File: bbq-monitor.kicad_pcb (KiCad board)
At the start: 4 copper layers, 48.5 x 43.3 mm, 51 parts, among them J1 Power, J2 USB_B_Mini, J3 Thermocouple, Q1 AO3401A, Q2 BC847, Q3 BC847, SW1 SW_Push, U1 ESP32-WROOM-32D, U2 TPS62132, U3 CP2104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

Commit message: Gave it a bit of a tidy up
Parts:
- removed the H4 at (190.8, 63.0)
- added H2: TL, MountingHole:MountingHole_3.2mm_M3_Pad_Via, F.Cu at (150.9, 62.7)
- R14: value 820k -> 82K
- R15: value 270k -> 27k
- moved H4 40.0 mm to (190.8, 63.0)
- moved R5 15.9 mm to (171.1, 83.4), turned to 90 degrees
- moved D2 14.0 mm to (173.1, 83.3)
- moved R12 2.45 mm to (187.7, 73.2), turned to 180 degrees
- moved C10 0.66 mm to (164.5, 95.3)
- moved R9 0.47 mm to (172.5, 65.8), turned to 270 degrees
- moved H1 0.08 mm to (151.0, 96.9), turned to 0 degrees
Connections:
- net Net-(D1-Pad2) renamed LED2
- D2 pad 2: Net-(D2-Pad2) -> LED1
- U1 pad 13: Net-(D2-Pad2) -> Net-(U1-Pad13)
- U1 pad 16: Net-(U1-Pad16) -> LED1
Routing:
- net Net-(D2-Pad2): track 16.3 -> 0.00 mm
- net +3V3: track 44.9 -> 51.9 mm, vias 13 -> 16
- net TEMP_HUMID_SEN: track 19.3 -> 14.3 mm
- net RESET: track 39.4 -> 44.1 mm
- net LED1: track 0.00 -> 3.44 mm
- net +5V: track 29.6 -> 27.4 mm
- net Net-(J3-Pad1): track 9.30 -> 7.73 mm
- net Net-(U1-Pad13): track 0.00 -> 0.61 mm
- net GND: vias 109 -> 141
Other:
- board text added: "ESP32-BBQ"

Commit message: updated gerbers
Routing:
- net /DIFF+: track 30.5 -> 31.9 mm
- net /DIFF-: track 29.5 -> 30.7 mm

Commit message: up
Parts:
- removed C10, C12, C14: 100n, Capacitor_SMD:C_0603_1608Metric
- removed C13, C15: 10n, Capacitor_SMD:C_0603_1608Metric
- removed C16: 100n, Capacitor_SMD:C_0402_1005Metric
- removed C17: 10u, Capacitor_SMD:C_0402_1005Metric
- removed H4: TR, MountingHole:MountingHole_3.2mm_M3_Pad_Via
- removed U5: AD8495, Package_SO:MSOP-8_3x3mm_P0.65mm
- removed U6: DHT11, Sensor:Aosong_DHT11_5.5x12.0_P2.54mm
- added C9: 100n, Capacitor_SMD:C_0603_1608Metric, F.Cu at (206.5, 86.8)
- added D3: RED, LED_SMD:LED_0603_1608Metric, F.Cu at (173.6, 113.1)
- added D4: RED, LED_SMD:LED_0603_1608Metric, F.Cu at (201.4, 113.4)
- added D5: RED, LED_SMD:LED_0603_1608Metric, F.Cu at (196.5, 113.4)
- added D6: D_Zener, Diode_SMD:D_1206_3216Metric, F.Cu at (169.7, 107.1)
- added D7: D_Schottky, Diode_SMD:D_1206_3216Metric, F.Cu at (173.2, 101.1)
- added IC1: MAX6675, hardware libraries:SO08, F.Cu at (202.9, 90.1)
- added Q4: AO3401A, Package_TO_SOT_SMD:SOT-23, F.Cu at (172.8, 104.0)
- J1: value Power -> Battery Power
- R10, R11, R9: value 1M -> 220
- R13: value 100 -> 10k
- moved H1 60.3 mm to (208.7, 114.3)
- moved R11 52.0 mm to (198.2, 113.4)
- moved J1 50.2 mm to (166.1, 112.0)
- moved R10 50.1 mm to (199.8, 113.4)
- moved R9 47.4 mm to (172.1, 113.2)
- moved J3 46.9 mm to (205.8, 97.7), turned to 90 degrees
- moved F1 44.2 mm to (166.2, 105.3), turned to 270 degrees
- moved J2 43.7 mm to (188.2, 110.5), turned to 0 degrees
- moved Q1 41.5 mm to (169.2, 104.0)
- moved C8 40.9 mm to (175.5, 108.5), turned to 270 degrees
- moved L1 39.9 mm to (179.9, 108.6)
- moved C1 39.7 mm to (175.3, 104.0), turned to 270 degrees
- moved U2 39.2 mm to (180.1, 104.8), turned to 180 degrees
- moved Q2 38.7 mm to (196.3, 102.8), turned to 90 degrees
- moved Q3 38.6 mm to (200.0, 102.8)
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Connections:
- net Net-(F1-Pad2) renamed BATT_PWR
- C1 pad 1: /BATT -> Net-(C1-Pad1)
- C2 pad 1: /BATT -> Net-(C1-Pad1)
- J2 pad 1: +5V -> USB_PWR
- J3 pad 1: Net-(J3-Pad1) -> GND
- J3 pad 2: Net-(J3-Pad2) -> Net-(IC1-Pad3)
- Q1 pad 2: /BATT -> BATT_SAFE
- R10 pad 1: Net-(J3-Pad2) -> TX_LED
- R10 pad 2: /Thermocouple_INPUT_FILTERED+ -> Net-(D4-Pad1)
- R11 pad 1: Net-(J3-Pad1) -> RX_LED
- R11 pad 2: /Thermocouple_INPUT_FILTERED- -> Net-(D5-Pad1)
- R12 pad 1: +3V3 -> GND
- R12 pad 2: TEMP_HUMID_SEN -> USB_PWR
- R14 pad 1: /BATT -> BATT_SAFE
- R9 pad 2: Net-(J3-Pad1) -> Net-(D3-Pad1)
- U1 pad 11: THERMOCOUPLE -> Net-(U1-Pad11)
- U1 pad 29: Net-(U1-Pad29) -> THERMO_SPI_CS
- U1 pad 30: Net-(U1-Pad30) -> THERMO_SPI_CLK
- U1 pad 31: Net-(U1-Pad31) -> THERMO_SPI_DO
- U1 pad 6: TEMP_HUMID_SEN -> Net-(U1-Pad6)
- U2 pad 10: /BATT -> Net-(C1-Pad1)
- U2 pad 11: /BATT -> Net-(C1-Pad1)
- U2 pad 12: /BATT -> Net-(C1-Pad1)
- U2 pad 13: /BATT -> Net-(C1-Pad1)
- U3 pad 13: Net-(U3-Pad13) -> RX_LED
- U3 pad 14: Net-(U3-Pad14) -> TX_LED
- U3 pad 8: +5V -> USB_PWR
- U4 pad 5: +5V -> USB_PWR
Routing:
- net USB_PWR: track 0.00 -> 51.1 mm
- net GND: track 71.2 -> 117.4 mm, vias 141 -> 68
- net /DIFF+: track 31.9 -> 2.22 mm
- net /DIFF-: track 30.7 -> 2.27 mm
- net +5V: track 27.4 -> 0.00 mm, vias 2 -> 0
- net /BATT: track 26.2 -> 0.00 mm
- net RX_CP+: track 1.78 -> 26.7 mm
- net GPIO0: track 30.3 -> 9.16 mm
- net TX_CP-: track 4.18 -> 24.9 mm
- net BATT_LEVEL: track 22.3 -> 3.78 mm
- net BATT_SAFE: track 0.00 -> 18.1 mm
- net TEMP_HUMID_SEN: track 14.3 -> 0.00 mm
- net Net-(C1-Pad1): track 0.00 -> 14.1 mm
- net D+: track 3.68 -> 15.7 mm, vias 0 -> 2
- net THERMO_SPI_DO: track 0.00 -> 10.2 mm
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- removed copper zone on B.Cu, net GND
- removed copper zone on F.Cu, net GND
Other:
- board size 48.5 x 43.3 mm -> 47 x 39.1 mm
- board text added: "BBQ-ESP32"
- board text added: "H.D."
- board text removed: "+"
- board text removed: "ESP32-BBQ"
- board text removed: "Harry Dobbs Version: 1.0"
- board text removed: "POWER"
- board text removed: "TEMP"

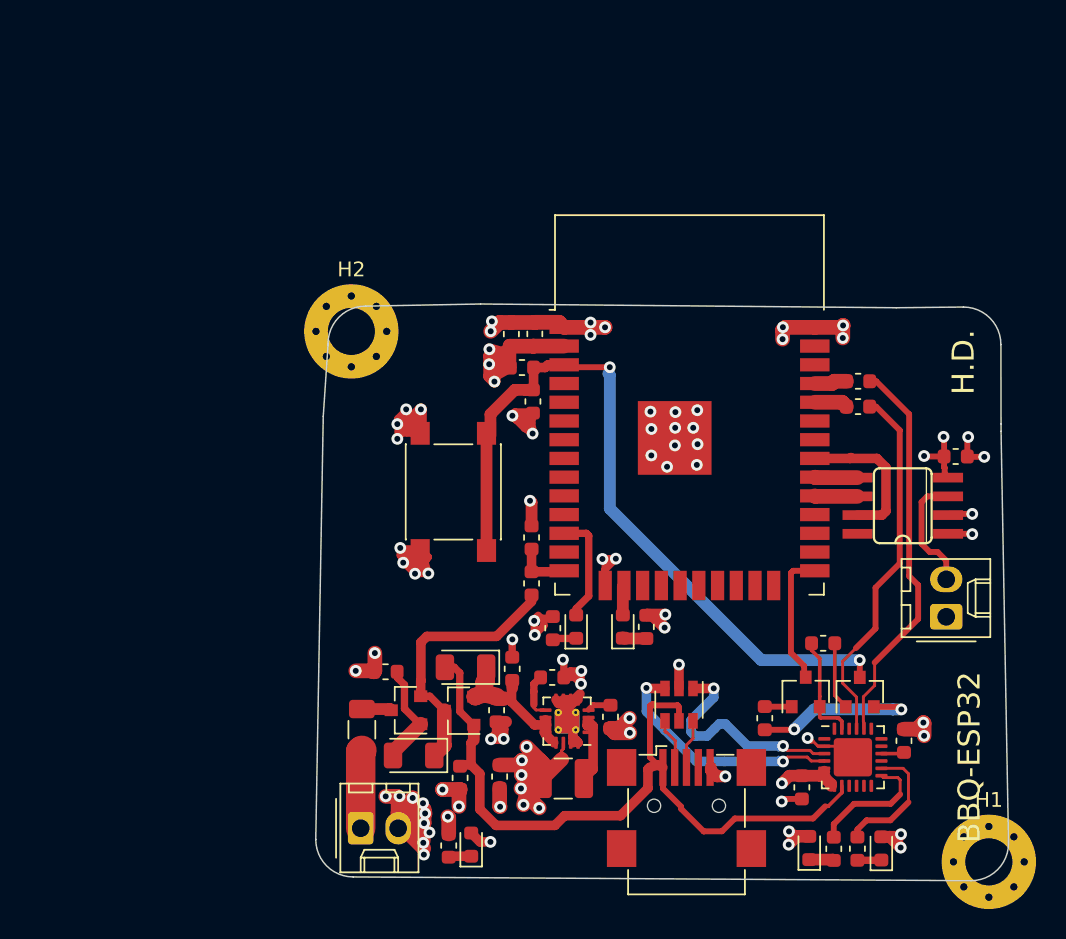
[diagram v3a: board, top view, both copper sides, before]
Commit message: dc-dc is too expexpesnive - project is on hold
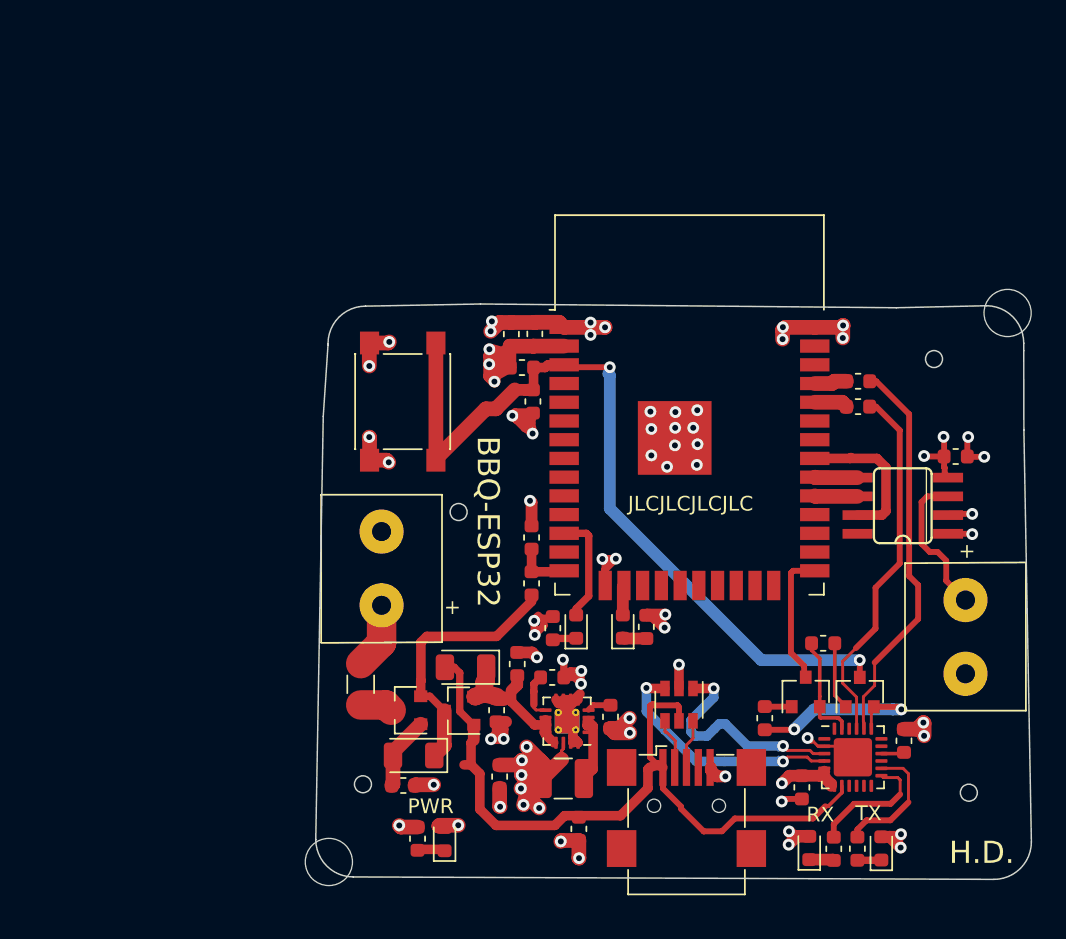
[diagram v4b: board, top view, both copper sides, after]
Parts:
- added G***: LOGO, hardware libraries:logo, B.Cu at (186.9, 95.7)
- H1, H2: footprint MountingHole:MountingHole_3.2mm_M3_Pad_Via -> MountingHole:MountingHole_3.2mm_M3
- J1, J3: footprint Connector_Molex:Molex_KK-254_AE-6410-02A_1x02_P2.54mm_Vertical -> rs-components:RS-Pro-5mm-Pitch-2-Pin-Terminal
- moved H1 37.3 mm to (210.0, 77.1)
- moved H2 36.0 mm to (164.0, 114.3)
- moved J1 17.7 mm to (167.5, 94.4), turned to 270 degrees
- moved R12 8.77 mm to (180.9, 112.1)
- moved R13 7.81 mm to (169.0, 109.1), turned to 180 degrees
- moved SW1 7.02 mm to (169.0, 83.1)
- moved F1 3.08 mm to (166.1, 102.3), turned to 90 degrees
- moved R9 2.17 mm to (170.0, 112.7)
- moved J3 1.89 mm to (207.1, 99.0)
- moved D3 1.84 mm to (171.8, 112.8)
- moved C2 0.47 mm to (176.7, 100.9)
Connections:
- F1 pad 2: BATT_PWR -> Net-(F1-Pad2)
- J1 pad 1: BATT_PWR -> GND
- J1 pad 2: GND -> Net-(F1-Pad2)
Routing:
- net GND: track 117.4 -> 78.8 mm, vias 68 -> 54
- net BATT_PWR: track 5.32 -> 0.00 mm
- net Net-(F1-Pad2): track 0.00 -> 4.55 mm
- net RESET: track 52.3 -> 55.4 mm
- net Net-(D6-Pad2): track 7.18 -> 5.02 mm
- net Net-(IC1-Pad3): track 8.21 -> 10.2 mm
- net RTS: track 11.8 -> 13.3 mm
- net Net-(C1-Pad1): track 14.1 -> 14.8 mm
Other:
- board size 47 x 39.1 mm -> 48.5 x 39 mm
- board text added: "+"
- board text added: "JLCJLCJLCJLC"
- board text added: "PWR"
- board text added: "RX"
- board text added: "TX"
